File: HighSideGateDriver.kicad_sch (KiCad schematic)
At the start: 7 parts, among them J4 LED, Q3 Q_NMOS_GDSD, U4 LTC4440ES6

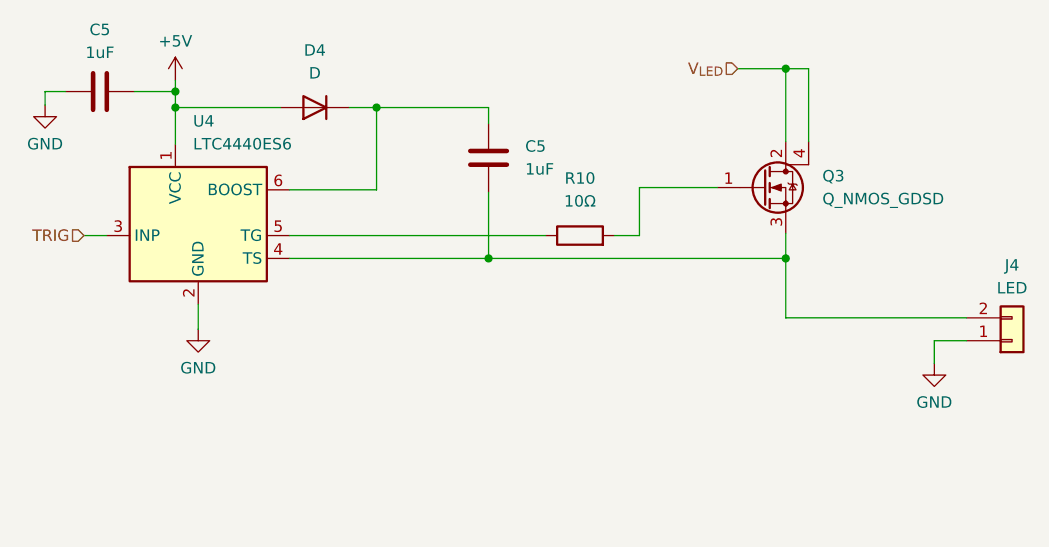
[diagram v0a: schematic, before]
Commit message: Added output capacitor to allow for smoothing of output voltage spike and an additional protection diode.
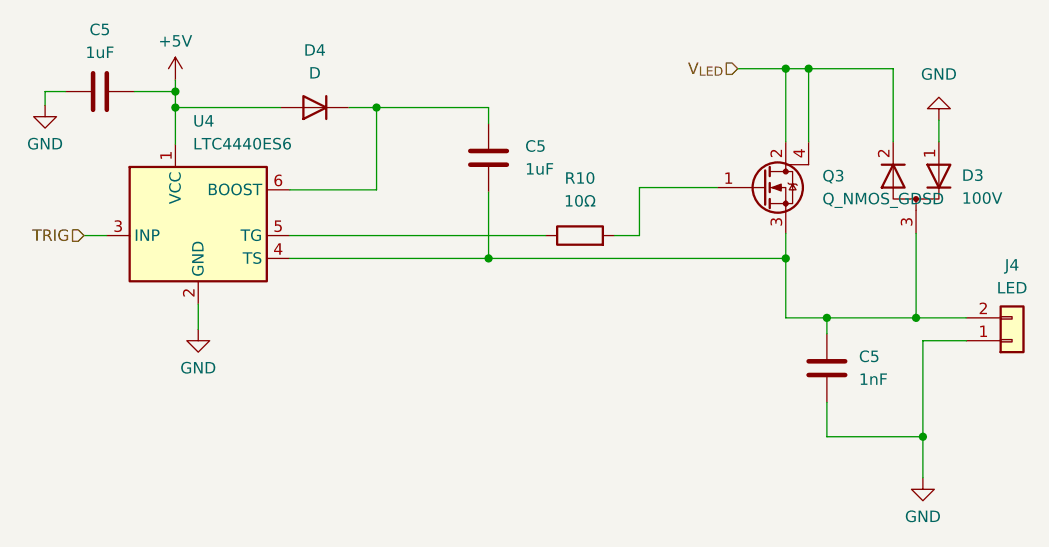
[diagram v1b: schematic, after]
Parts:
- added C5: 1nF, Capacitor_SMD:C_0805_2012Metric_Pad1.18x1.45mm_HandSolder, symbol Device:C
- added D3: 100V, Package_TO_SOT_SMD:SOT-23-3, symbol Device:D_Dual_Series_AKC_Parallel
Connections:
- net GND: now also C5.2, D3.1 (K)
- net V_{LED}: now also D3.2 (K)
- net at C5.2, J4.2 (Pin_2), Q3.3 (S)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: now also C5.1, D3.3 (A)
